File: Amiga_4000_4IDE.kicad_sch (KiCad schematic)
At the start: 11 parts, among them J1 AMIGA 4000, J2 CHANNEL 0, J3 CHANNEL 0

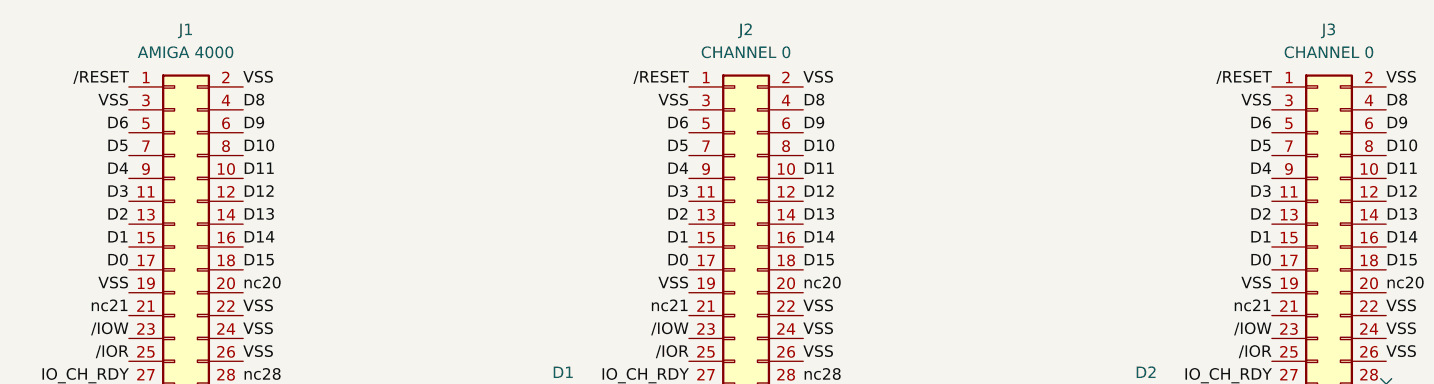
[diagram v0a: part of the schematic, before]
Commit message: Connect D7 (oops) and relayout PCB
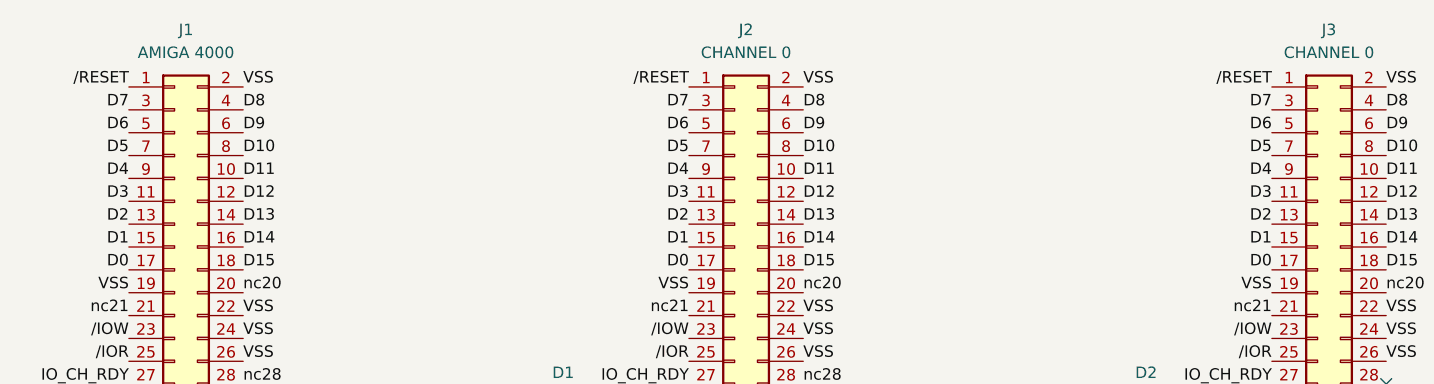
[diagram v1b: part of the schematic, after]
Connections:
- net VSS: no longer J1.3 (Pin_3), J2.3 (Pin_3), J3.3 (Pin_3)
- new net D7: J1.3 (Pin_3), J2.3 (Pin_3), J3.3 (Pin_3)
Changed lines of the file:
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@@
 		)
 	)
-	(label "VSS"
+	(label "D7"
 		(at 73.66 57.15 180)
 		(fields_autoplaced yes)
@@
 		)
 	)
-	(label "VSS"
+	(label "D7"
 		(at 135.89 57.15 180)
 		(fields_autoplaced yes)
@@
 		)
 	)
-	(label "VSS"
+	(label "D7"
 		(at 200.66 57.15 180)
 		(fields_autoplaced yes)
